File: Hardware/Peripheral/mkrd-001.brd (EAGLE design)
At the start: 18 x 31 mm, 5 parts

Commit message: First try.
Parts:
- removed S1, S2: (no value), switch-dil:A1353HEX
- added J1: MKR, SparkFun-Connectors:JST-5-PTH
- JP1: value (none) -> DISP; device pinhead:2X08 -> SparkFun-Connectors:1X04
- moved U$1 18.4 mm to (12.5, 7.00), turned to 0 degrees
- moved JP1 14.9 mm to (8.69, 1.27), turned to 0 degrees
- moved LOGO1 8.08 mm to (12.5, 13.0), turned to 0 degrees
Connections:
- removed net ANLG0: JP1.3, S2.1
- removed net ANLG1: JP1.7, S2.4
- removed net ANLG2: JP1.11, S2.8
- removed net ANLG3: JP1.15, S2.2
- removed net DTCT0: JP1.2, S1.1
- removed net DTCT1: JP1.6, S1.4
- removed net DTCT2: JP1.10, S1.8
- removed net DTCT3: JP1.14, S1.2
- new net SCL: J1.3, JP1.3
- new net SDA: J1.2, JP1.4
- net GND: now also J1.1; no longer JP1.13, JP1.5, JP1.9, S1.C
- net VCC: now also J1.5, JP1.2; no longer JP1.12, JP1.16, JP1.4, JP1.8, S2.C
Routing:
- net DTCT3: track 20.4 -> 0.00 mm
- net ANLG0: track 19.9 -> 0.00 mm
- net SDA: track 0.00 -> 19.5 mm
- net SCL: track 0.00 -> 19.3 mm
- net ANLG1: track 16.4 -> 0.00 mm
- net DTCT2: track 15.0 -> 0.00 mm
- net ANLG3: track 14.8 -> 0.00 mm
- net VCC: track 31.7 -> 19.9 mm
- net DTCT1: track 10.1 -> 0.00 mm
- net DTCT0: track 8.95 -> 0.00 mm
- net ANLG2: track 7.60 -> 0.00 mm
- net GND: track 28.5 -> 24.8 mm
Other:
- board size 18 x 31 mm -> 25 x 26 mm
- board text added: "5V"
- board text added: "MKR Display 0.0.1-X"
- board text added: "SC"
- board text added: "SD"
- board text removed: "A0"
- board text removed: "A1"
- board text removed: "A2"
- board text removed: "A3"
- board text removed: "D10"
- board text removed: "D12"
- board text removed: "D6"
- board text removed: "D9"
- board text removed: "Hex Sw 0.0.1-X"
- board text removed: "V/2"

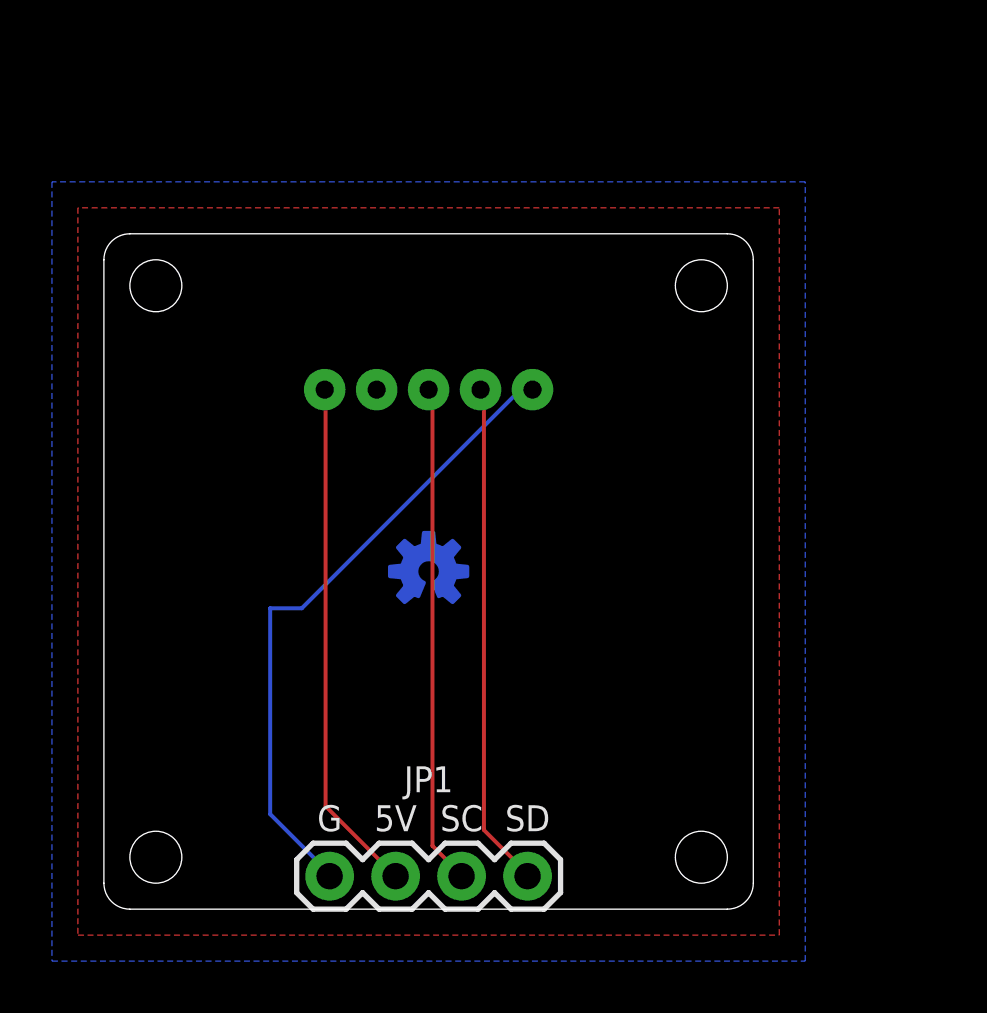
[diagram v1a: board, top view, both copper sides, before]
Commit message: Flipped MKR con.
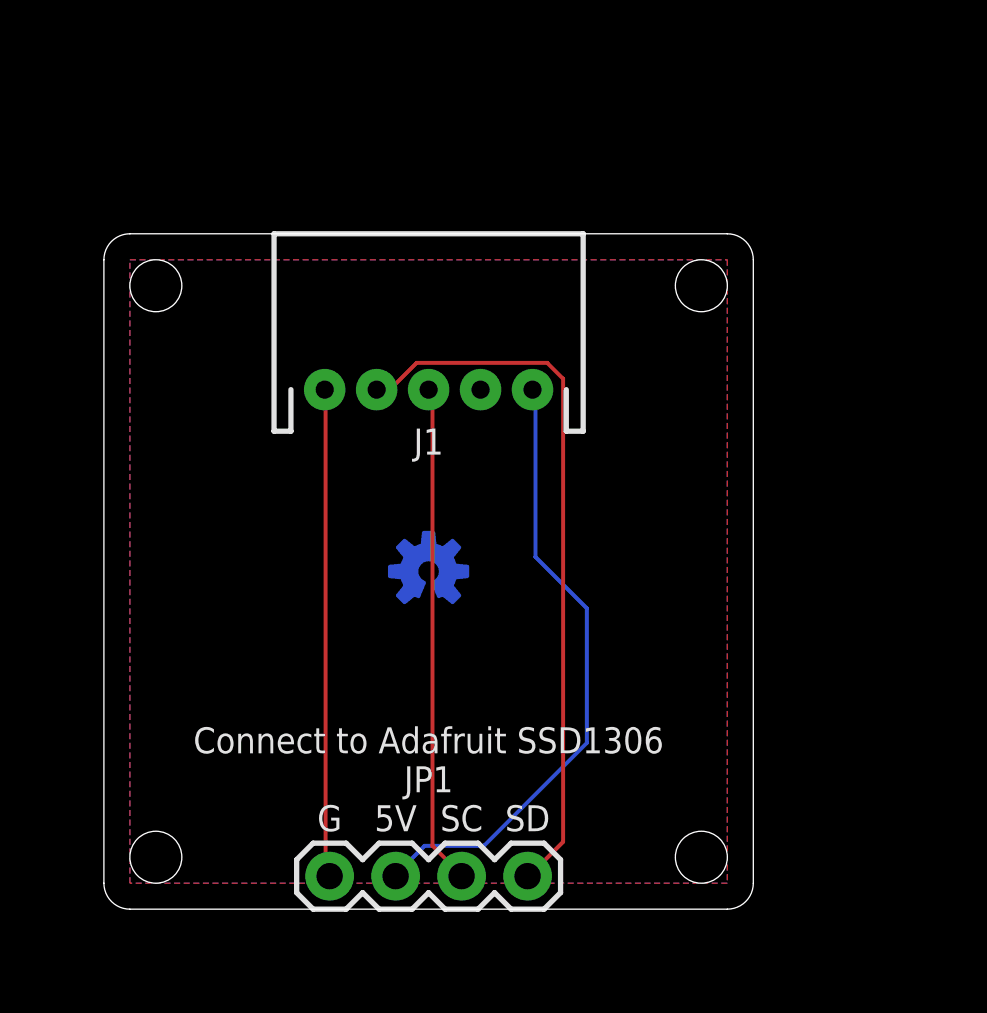
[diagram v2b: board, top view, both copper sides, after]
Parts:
- flipped J1 to the top
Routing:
- net SDA: track 19.5 -> 27.6 mm
- net GND: track 24.8 -> 18.8 mm
- net VCC: track 19.9 -> 24.0 mm
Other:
- board text added: "Connect to Adafruit SSD1306"
- board text added: "MKR"
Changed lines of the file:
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@@
 <rectangle x1="0" y1="0" x2="1" y2="26" layer="42"/>
 <hole x="2" y="2" drill="2"/>
-<circle x="23" y="2" radius="1.2" width="0.2" layer="42"/>
-<circle x="2" y="2" radius="1.2" width="0.2" layer="41"/>
+<circle x="23" y="2" radius="1.8" width="0.2" layer="42"/>
+<circle x="2" y="2" radius="1.8" width="0.2" layer="41"/>
 <rectangle x1="0" y1="0" x2="1" y2="26" layer="41"/>
 <rectangle x1="0" y1="25" x2="25" y2="26" layer="41"/>
@@
 <hole x="23" y="24" drill="2"/>
 <hole x="2" y="24" drill="2"/>
-<circle x="2" y="24" radius="1.2" width="0.2" layer="42"/>
-<circle x="2" y="2" radius="1.2" width="0.2" layer="42"/>
-<circle x="23" y="24" radius="1.2" width="0.2" layer="42"/>
-<circle x="2" y="24" radius="1.2" width="0.2" layer="41"/>
-<circle x="23" y="24" radius="1.2" width="0.2" layer="41"/>
-<circle x="23" y="2" radius="1.2" width="0.2" layer="41"/>
+<circle x="2" y="24" radius="1.8" width="0.2" layer="42"/>
+<circle x="2" y="2" radius="1.8" width="0.2" layer="42"/>
+<circle x="23" y="24" radius="1.8" width="0.2" layer="42"/>
+<circle x="2" y="24" radius="1.8" width="0.2" layer="41"/>
+<circle x="23" y="24" radius="1.8" width="0.2" layer="41"/>
+<circle x="23" y="2" radius="1.8" width="0.2" layer="41"/>
 <text x="8.69" y="3.5" size="1" layer="25" align="center">G</text>
 <text x="11.23" y="3.5" size="1" layer="25" align="center">5V</text>
@@
 <rectangle x1="17.5" y1="0" x2="25" y2="1" layer="41"/>
 <rectangle x1="6.5" y1="6.5" x2="18.5" y2="11.5" layer="42"/>
+<text x="12.5" y="24.5" size="1" layer="26" rot="MR0" align="center">MKR</text>
+<text x="12.5" y="6.5" size="1" layer="25" align="center">Connect to Adafruit SSD1306</text>
 </plain>
 <attributes>
@@
 <attribute name="VALUE" x="7.42" y="-0.762" size="0.6096" layer="27" font="vector" ratio="20"/>
 </element>
-<element name="J1" library="SparkFun-Connectors" library_urn="urn:adsk.eagle:library:513" package="JST-5-PTH" package3d_urn="urn:adsk.eagle:package:38120/1" value="MKR" x="12.5" y="20" smashed="yes" rot="MR0">
-<attribute name="NAME" x="12.5" y="18" size="1" layer="26" ratio="20" rot="MR0" align="center"/>
-<attribute name="SF_ID" value="PRT-09917" x="12.5" y="20" size="1.778" layer="28" rot="MR0" display="off"/>
-<attribute name="VALUE" x="14.151" y="22.413" size="0.6096" layer="28" font="vector" ratio="20" rot="MR0"/>
+<element name="J1" library="SparkFun-Connectors" library_urn="urn:adsk.eagle:library:513" package="JST-5-PTH" package3d_urn="urn:adsk.eagle:package:38120/1" value="MKR" x="12.5" y="20" smashed="yes">
+<attribute name="NAME" x="12.5" y="18" size="1" layer="25" ratio="20" align="center"/>
+<attribute name="SF_ID" value="PRT-09917" x="12.5" y="20" size="1.778" layer="27" display="off"/>
+<attribute name="VALUE" x="10.849" y="22.413" size="0.6096" layer="27" font="vector" ratio="20"/>
 </element>
 </elements>
@@
 <contactref element="JP1" pad="1"/>
 <contactref element="J1" pad="1"/>
-<wire x1="16.002" y1="19.9644" x2="16.4592" y2="19.9644" width="0.1524" layer="16"/>
-<wire x1="7.62" y1="11.5824" x2="16.002" y2="19.9644" width="0.1524" layer="16"/>
-<wire x1="6.4008" y1="11.5824" x2="7.62" y2="11.5824" width="0.1524" layer="16"/>
-<wire x1="6.4008" y1="3.6576" x2="6.4008" y2="11.5824" width="0.1524" layer="16"/>
-<wire x1="8.6868" y1="1.3716" x2="6.4008" y2="3.6576" width="0.1524" layer="16"/>
-<wire x1="16.4592" y1="19.9644" x2="16.5" y2="20" width="0.1524" layer="16"/>
-<wire x1="8.6868" y1="1.3716" x2="8.69" y2="1.27" width="0.1524" layer="16"/>
+<wire x1="8.5344" y1="1.524" x2="8.5344" y2="19.9644" width="0.1524" layer="1"/>
+<wire x1="8.6868" y1="1.3716" x2="8.5344" y2="1.524" width="0.1524" layer="1"/>
+<wire x1="8.5344" y1="19.9644" x2="8.5" y2="20" width="0.1524" layer="1"/>
+<wire x1="8.6868" y1="1.3716" x2="8.69" y2="1.27" width="0.1524" layer="1"/>
 <polygon width="0.2" layer="1">
-<vertex x="-1" y="-1"/>
-<vertex x="26" y="-1"/>
-<vertex x="26" y="27"/>
-<vertex x="-1" y="27"/>
+<vertex x="1" y="25"/>
+<vertex x="24" y="25"/>
+<vertex x="24" y="1"/>
+<vertex x="1" y="1"/>
 </polygon>
 <polygon width="0.2" layer="16">
-<vertex x="-2" y="-2"/>
-<vertex x="27" y="-2"/>
-<vertex x="27" y="28"/>
-<vertex x="-2" y="28"/>
+<vertex x="1" y="25"/>
+<vertex x="24" y="25"/>
+<vertex x="24" y="1"/>
+<vertex x="1" y="1"/>
 </polygon>
 </signal>
@@
 <contactref element="JP1" pad="2"/>
 <contactref element="J1" pad="5"/>
-<wire x1="8.5344" y1="3.9624" x2="8.5344" y2="19.9644" width="0.1524" layer="1"/>
-<wire x1="11.1252" y1="1.3716" x2="8.5344" y2="3.9624" width="0.1524" layer="1"/>
-<wire x1="8.5344" y1="19.9644" x2="8.5" y2="20" width="0.1524" layer="1"/>
-<wire x1="11.1252" y1="1.3716" x2="11.23" y2="1.27" width="0.1524" layer="1"/>
+<wire x1="16.6116" y1="13.5636" x2="16.6116" y2="19.9644" width="0.1524" layer="16"/>
+<wire x1="18.5928" y1="11.5824" x2="16.6116" y2="13.5636" width="0.1524" layer="16"/>
+<wire x1="18.5928" y1="6.4008" x2="18.5928" y2="11.5824" width="0.1524" layer="16"/>
+<wire x1="14.6304" y1="2.4384" x2="18.5928" y2="6.4008" width="0.1524" layer="16"/>
+<wire x1="12.3444" y1="2.4384" x2="14.6304" y2="2.4384" width="0.1524" layer="16"/>
+<wire x1="11.2776" y1="1.3716" x2="12.3444" y2="2.4384" width="0.1524" layer="16"/>
+<wire x1="16.6116" y1="19.9644" x2="16.5" y2="20" width="0.1524" layer="16"/>
+<wire x1="11.2776" y1="1.3716" x2="11.23" y2="1.27" width="0.1524" layer="16"/>
 </signal>
 <signal name="SCL">
@@
 <contactref element="JP1" pad="4"/>
 <contactref element="J1" pad="2"/>
-<wire x1="14.6304" y1="3.048" x2="14.6304" y2="19.9644" width="0.1524" layer="1"/>
-<wire x1="16.3068" y1="1.3716" x2="14.6304" y2="3.048" width="0.1524" layer="1"/>
-<wire x1="14.6304" y1="19.9644" x2="14.5" y2="20" width="0.1524" layer="1"/>
-<wire x1="16.3068" y1="1.3716" x2="16.31" y2="1.27" width="0.1524" layer="1"/>
+<wire x1="11.1252" y1="20.1168" x2="10.5156" y2="20.1168" width="0.1524" layer="1"/>
+<wire x1="12.0396" y1="21.0312" x2="11.1252" y2="20.1168" width="0.1524" layer="1"/>
+<wire x1="17.0688" y1="21.0312" x2="12.0396" y2="21.0312" width="0.1524" layer="1"/>
+<wire x1="17.6784" y1="20.4216" x2="17.0688" y2="21.0312" width="0.1524" layer="1"/>
+<wire x1="17.6784" y1="2.5908" x2="17.6784" y2="20.4216" width="0.1524" layer="1"/>
+<wire x1="16.4592" y1="1.3716" x2="17.6784" y2="2.5908" width="0.1524" layer="1"/>
+<wire x1="10.5156" y1="20.1168" x2="10.5" y2="20" width="0.1524" layer="1"/>
+<wire x1="16.4592" y1="1.3716" x2="16.31" y2="1.27" width="0.1524" layer="1"/>
 </signal>
 </signals>

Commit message: Added cap.
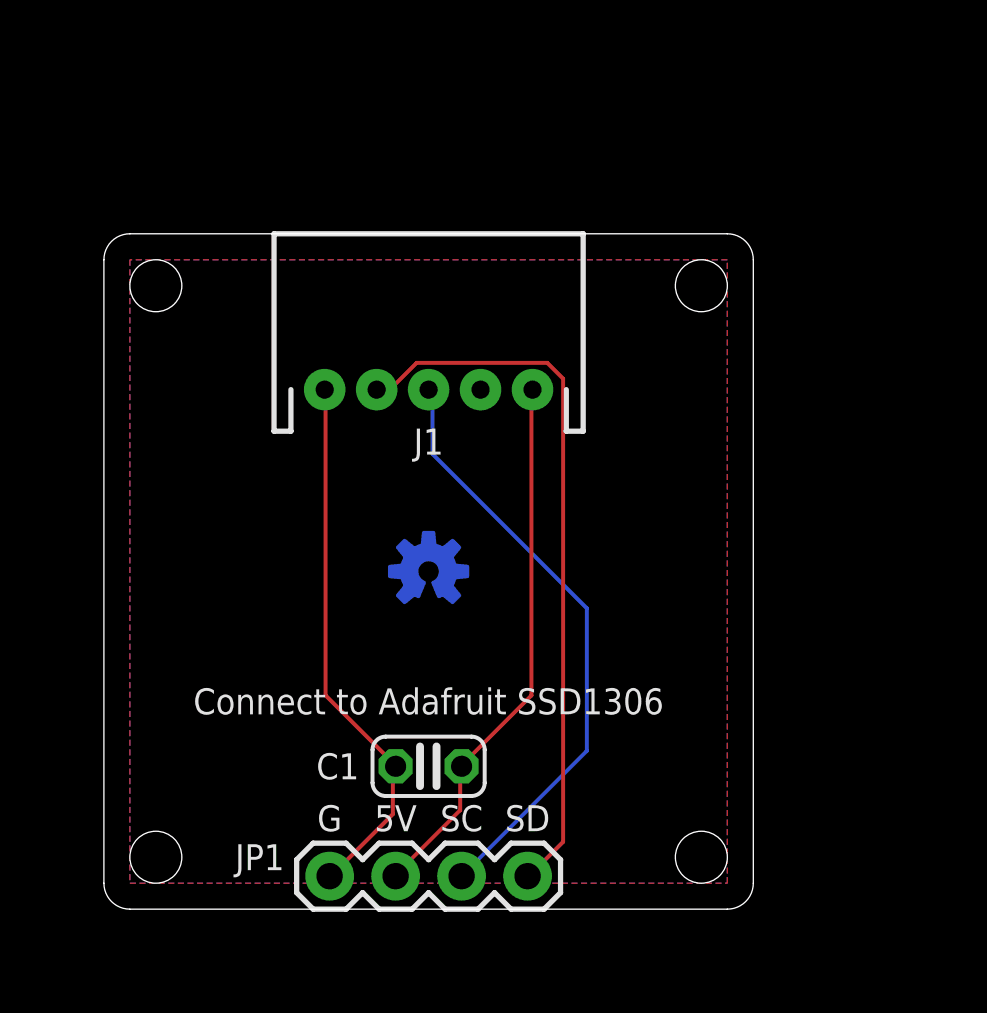
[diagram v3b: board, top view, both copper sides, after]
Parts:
- added C1: (no value), rcl:C025-024X044
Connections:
- net GND: now also C1.2
- net VCC: now also C1.1
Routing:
- net SCL: track 19.3 -> 23.3 mm
- net VCC: track 24.0 -> 20.9 mm
- net GND: track 18.8 -> 21.0 mm
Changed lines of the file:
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@@
 <layer number="20" name="Dimension" color="24" fill="1" visible="yes" active="yes"/>
 <layer number="21" name="tPlace" color="7" fill="1" visible="yes" active="yes"/>
-<layer number="22" name="bPlace" color="7" fill="1" visible="yes" active="yes"/>
+<layer number="22" name="bPlace" color="7" fill="1" visible="no" active="yes"/>
 <layer number="23" name="tOrigins" color="15" fill="1" visible="yes" active="yes"/>
 <layer number="24" name="bOrigins" color="15" fill="1" visible="yes" active="yes"/>
 <layer number="25" name="tNames" color="7" fill="1" visible="yes" active="yes"/>
-<layer number="26" name="bNames" color="7" fill="1" visible="yes" active="yes"/>
+<layer number="26" name="bNames" color="7" fill="1" visible="no" active="yes"/>
 <layer number="27" name="tValues" color="7" fill="1" visible="no" active="yes"/>
 <layer number="28" name="bValues" color="7" fill="1" visible="no" active="yes"/>
@@
 <rectangle x1="6.5" y1="6.5" x2="18.5" y2="11.5" layer="42"/>
 <text x="12.5" y="24.5" size="1" layer="26" rot="MR0" align="center">MKR</text>
-<text x="12.5" y="6.5" size="1" layer="25" align="center">Connect to Adafruit SSD1306</text>
+<text x="12.5" y="8" size="1" layer="25" align="center">Connect to Adafruit SSD1306</text>
 </plain>
 <attributes>
@@
 <element name="U$1" library="pineapple" package="PINEAPPLE450_SILK" value="PINEAPPLE450_SILK" x="12.5" y="7" smashed="yes" rot="MR0"/>
 <element name="JP1" library="SparkFun-Connectors" library_urn="urn:adsk.eagle:library:513" package="1X04" package3d_urn="urn:adsk.eagle:package:38085/1" value="DISP" x="8.69" y="1.27" smashed="yes">
-<attribute name="NAME" x="12.5" y="5" size="1" layer="25" ratio="20" align="center"/>
+<attribute name="NAME" x="6" y="2" size="1" layer="25" ratio="20" align="center"/>
 <attribute name="PROD_ID" value="CONN-09696" x="8.69" y="1.27" size="1.778" layer="27" display="off"/>
 <attribute name="VALUE" x="7.42" y="-0.762" size="0.6096" layer="27" font="vector" ratio="20"/>
@@
 <attribute name="VALUE" x="10.849" y="22.413" size="0.6096" layer="27" font="vector" ratio="20"/>
 </element>
+<element name="C1" library="rcl" library_urn="urn:adsk.eagle:library:334" package="C025-024X044" package3d_urn="urn:adsk.eagle:package:23630/1" value="" x="12.5" y="5.5" smashed="yes" rot="R180">
+<attribute name="NAME" x="9" y="5.5" size="1" layer="25" ratio="10" align="center"/>
+<attribute name="POPULARITY" value="56" x="12.5" y="5.5" size="1.778" layer="27" rot="R180" display="off"/>
+<attribute name="SPICEPREFIX" value="C" x="12.5" y="5.5" size="1.778" layer="27" rot="R180" display="off"/>
+<attribute name="VALUE" x="14.278" y="8.167" size="1.27" layer="27" ratio="10" rot="R180"/>
+</element>
 </elements>
 <signals>
@@
 <contactref element="JP1" pad="1"/>
 <contactref element="J1" pad="1"/>
-<wire x1="8.5344" y1="1.524" x2="8.5344" y2="19.9644" width="0.1524" layer="1"/>
-<wire x1="8.6868" y1="1.3716" x2="8.5344" y2="1.524" width="0.1524" layer="1"/>
+<contactref element="C1" pad="2"/>
+<wire x1="11.1252" y1="3.6576" x2="11.1252" y2="5.4864" width="0.1524" layer="1"/>
+<wire x1="8.8392" y1="1.3716" x2="11.1252" y2="3.6576" width="0.1524" layer="1"/>
+<wire x1="11.1252" y1="5.4864" x2="11.23" y2="5.5" width="0.1524" layer="1"/>
+<wire x1="8.8392" y1="1.3716" x2="8.69" y2="1.27" width="0.1524" layer="1"/>
+<wire x1="8.5344" y1="8.2296" x2="8.5344" y2="19.9644" width="0.1524" layer="1"/>
+<wire x1="11.1252" y1="5.6388" x2="8.5344" y2="8.2296" width="0.1524" layer="1"/>
 <wire x1="8.5344" y1="19.9644" x2="8.5" y2="20" width="0.1524" layer="1"/>
-<wire x1="8.6868" y1="1.3716" x2="8.69" y2="1.27" width="0.1524" layer="1"/>
+<wire x1="11.1252" y1="5.6388" x2="11.23" y2="5.5" width="0.1524" layer="1"/>
 <polygon width="0.2" layer="1">
+<vertex x="1" y="1"/>
+<vertex x="24" y="1"/>
+<vertex x="24" y="25"/>
 <vertex x="1" y="25"/>
-<vertex x="24" y="25"/>
-<vertex x="24" y="1"/>
-<vertex x="1" y="1"/>
 </polygon>
 <polygon width="0.2" layer="16">
+<vertex x="1" y="1"/>
+<vertex x="24" y="1"/>
+<vertex x="24" y="25"/>
 <vertex x="1" y="25"/>
-<vertex x="24" y="25"/>
-<vertex x="24" y="1"/>
-<vertex x="1" y="1"/>
 </polygon>
 </signal>
@@
 <contactref element="JP1" pad="2"/>
 <contactref element="J1" pad="5"/>
-<wire x1="16.6116" y1="13.5636" x2="16.6116" y2="19.9644" width="0.1524" layer="16"/>
-<wire x1="18.5928" y1="11.5824" x2="16.6116" y2="13.5636" width="0.1524" layer="16"/>
-<wire x1="18.5928" y1="6.4008" x2="18.5928" y2="11.5824" width="0.1524" layer="16"/>
-<wire x1="14.6304" y1="2.4384" x2="18.5928" y2="6.4008" width="0.1524" layer="16"/>
-<wire x1="12.3444" y1="2.4384" x2="14.6304" y2="2.4384" width="0.1524" layer="16"/>
-<wire x1="11.2776" y1="1.3716" x2="12.3444" y2="2.4384" width="0.1524" layer="16"/>
-<wire x1="16.6116" y1="19.9644" x2="16.5" y2="20" width="0.1524" layer="16"/>
-<wire x1="11.2776" y1="1.3716" x2="11.23" y2="1.27" width="0.1524" layer="16"/>
+<contactref element="C1" pad="1"/>
+<wire x1="13.716" y1="3.81" x2="13.716" y2="5.4864" width="0.1524" layer="1"/>
+<wire x1="11.2776" y1="1.3716" x2="13.716" y2="3.81" width="0.1524" layer="1"/>
+<wire x1="13.716" y1="5.4864" x2="13.77" y2="5.5" width="0.1524" layer="1"/>
+<wire x1="11.2776" y1="1.3716" x2="11.23" y2="1.27" width="0.1524" layer="1"/>
+<wire x1="16.4592" y1="8.2296" x2="16.4592" y2="19.9644" width="0.1524" layer="1"/>
+<wire x1="13.8684" y1="5.6388" x2="16.4592" y2="8.2296" width="0.1524" layer="1"/>
+<wire x1="16.4592" y1="19.9644" x2="16.5" y2="20" width="0.1524" layer="1"/>
+<wire x1="13.8684" y1="5.6388" x2="13.77" y2="5.5" width="0.1524" layer="1"/>
 </signal>
 <signal name="SCL">
 <contactref element="JP1" pad="3"/>
 <contactref element="J1" pad="3"/>
-<wire x1="12.6492" y1="2.4384" x2="12.6492" y2="19.9644" width="0.1524" layer="1"/>
-<wire x1="13.716" y1="1.3716" x2="12.6492" y2="2.4384" width="0.1524" layer="1"/>
-<wire x1="12.6492" y1="19.9644" x2="12.5" y2="20" width="0.1524" layer="1"/>
-<wire x1="13.716" y1="1.3716" x2="13.77" y2="1.27" width="0.1524" layer="1"/>
+<wire x1="12.6492" y1="17.526" x2="12.6492" y2="19.9644" width="0.1524" layer="16"/>
+<wire x1="18.5928" y1="11.5824" x2="12.6492" y2="17.526" width="0.1524" layer="16"/>
+<wire x1="18.5928" y1="6.096" x2="18.5928" y2="11.5824" width="0.1524" layer="16"/>
+<wire x1="13.8684" y1="1.3716" x2="18.5928" y2="6.096" width="0.1524" layer="16"/>
+<wire x1="12.6492" y1="19.9644" x2="12.5" y2="20" width="0.1524" layer="16"/>
+<wire x1="13.8684" y1="1.3716" x2="13.77" y2="1.27" width="0.1524" layer="16"/>
 </signal>
 <signal name="SDA">

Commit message: Added new board.
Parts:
- removed JP1: DISP, SparkFun-Connectors:1X04
- added C2, C3: 1u, rcl:C025-025X050
- added R1: 1.5k, rcl:0204/5
- added R2: 3.3k, rcl:0204/5
- added R3, R4: 10k, rcl:0204/5
- added X1: AQM0802A-RN-GBW, AQM0802A-RN-GBW:AQM0802A-RN-GBW-FOOTPRINT
- C1: value (none) -> 0.1u
- moved J1 6.95 mm to (16.0, 26.0)
- moved C1 4.95 mm to (16.0, 2.00)
- moved LOGO1 4.61 mm to (16.0, 16.0)
- moved U$1 4.61 mm to (16.0, 10.0)
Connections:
- new net 3V3: C1.1, C2.1, R1.2, R2.2, R3.1, R4.1, X1.5, X1.9
- new net N$1: C2.2, X1.2
- new net N$2: C3.2, X1.4
- new net N$3: C3.1, X1.3
- net GND: now also R2.1, X1.6; no longer JP1.1
- net SCL: now also R3.2, X1.8; no longer JP1.3
- net SDA: now also R4.2, X1.7; no longer JP1.4
- net VCC: now also R1.1; no longer C1.1, JP1.2
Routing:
- net 3V3: track 0.00 -> 100.0 mm
- net GND: track 21.0 -> 41.1 mm
- net N$2: track 0.00 -> 12.6 mm
- net N$3: track 0.00 -> 11.6 mm
- net SDA: track 27.6 -> 38.7 mm
- net SCL: track 23.3 -> 33.1 mm
- net VCC: track 20.9 -> 15.4 mm
- net N$1: track 0.00 -> 4.06 mm
- removed copper zone on layer 1, net GND
- removed copper zone on layer 16, net GND
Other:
- board size 25 x 26 mm -> 32 x 32 mm
- board text removed: "5V"
- board text removed: "Connect to Adafruit SSD1306"
- board text removed: "G"
- board text removed: "SC"
- board text removed: "SD"
